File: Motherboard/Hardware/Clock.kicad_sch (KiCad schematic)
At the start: 18 parts, among them Q46 BC858, Q50 BC858, Q51 BC858

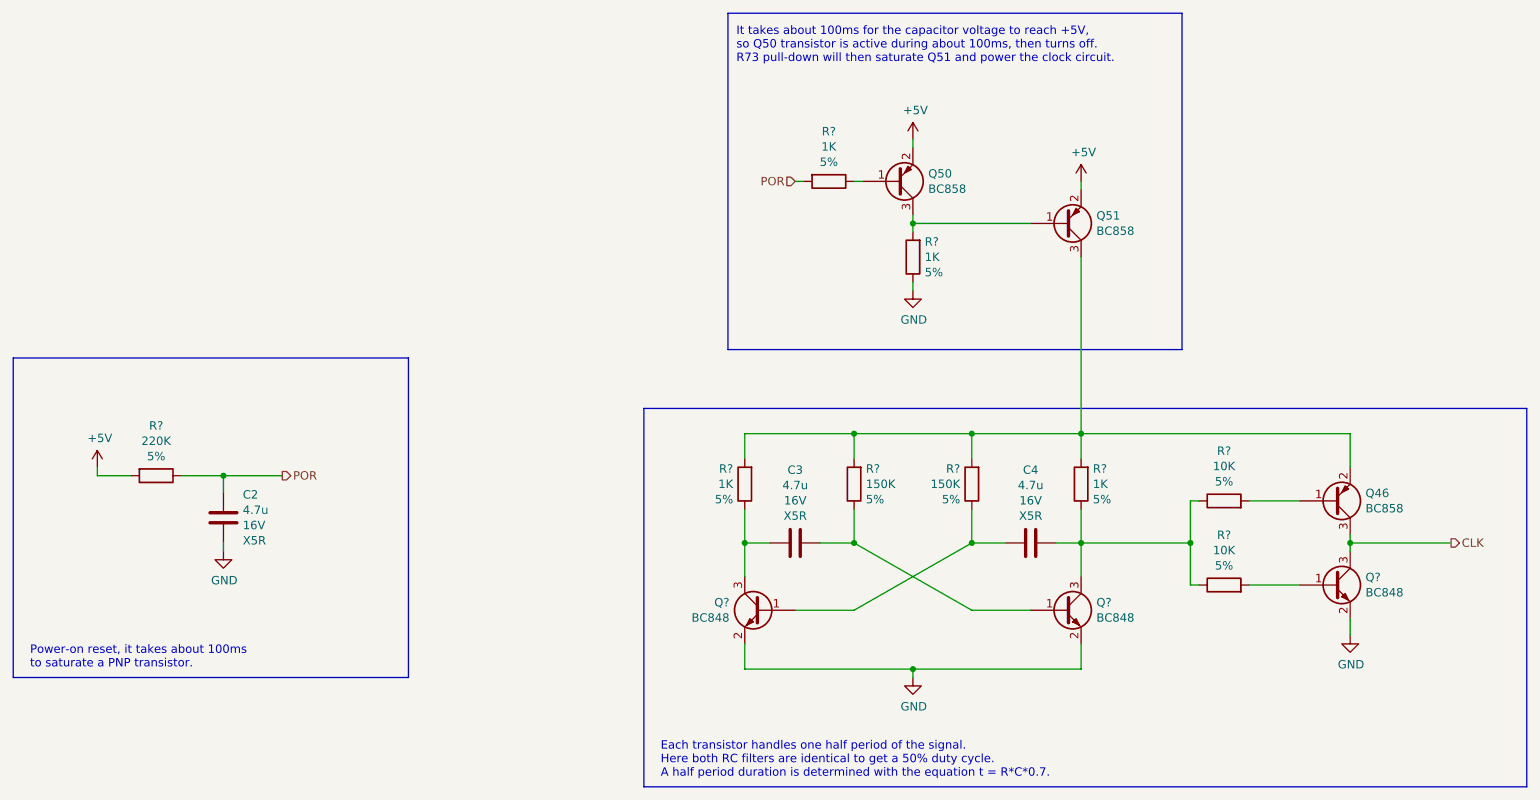
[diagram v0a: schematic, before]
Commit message: Updated the motherboard PCB to KiCad 7.
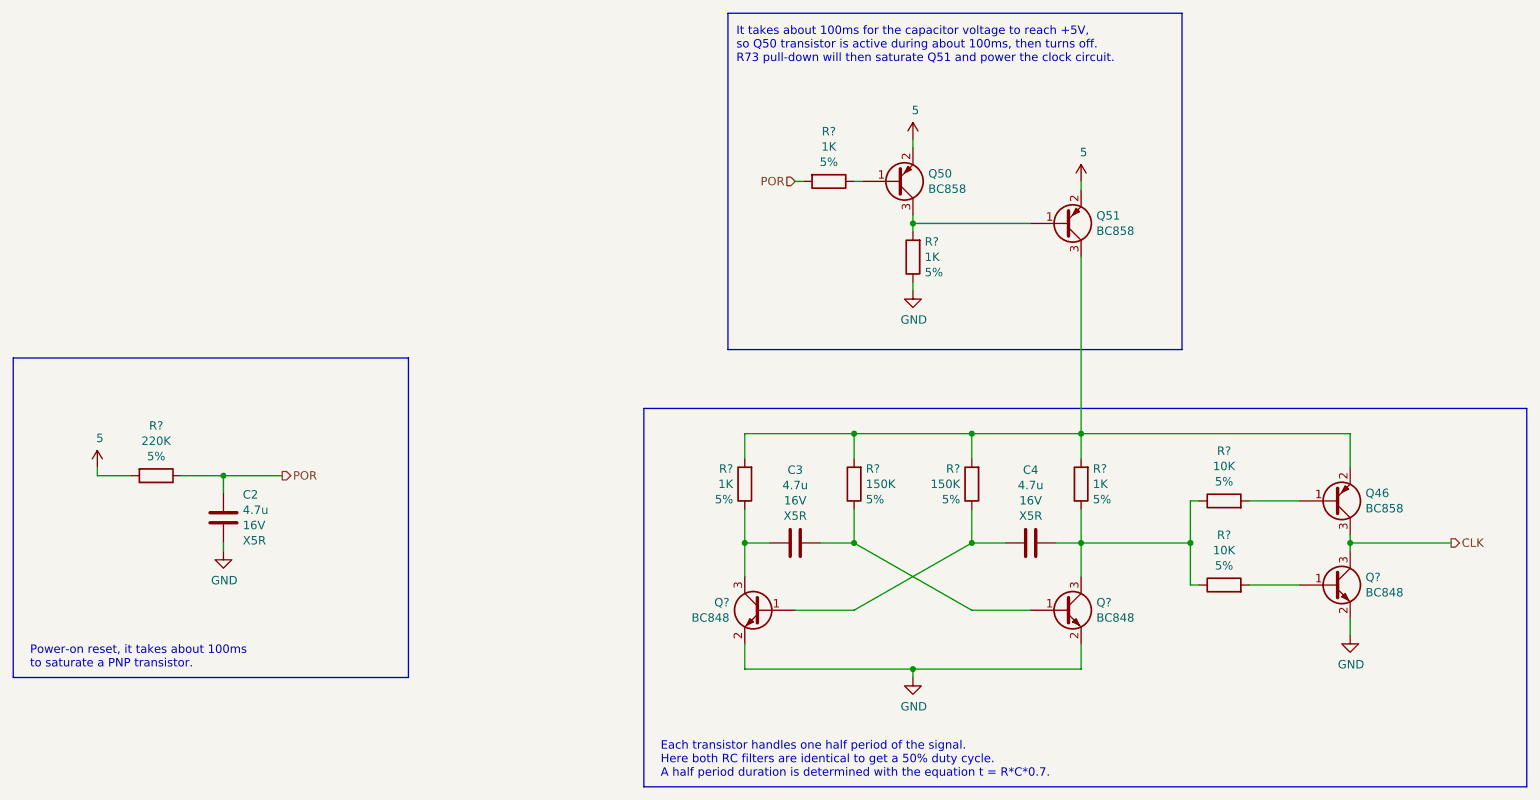
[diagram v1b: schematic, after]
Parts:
- Q46, Q50, Q51: Spice_Lib_File Spice_Simulation/BC858.lib -> (none); Spice_Model BC858 -> (none); Spice_Netlist_Enabled Y -> (none); Spice_Node_Sequence 3 1 2 -> (none); Spice_Primitive Q -> (none)
- Q? (x3): Spice_Lib_File Spice_Simulation/BC848.lib -> (none); Spice_Model BC848 -> (none); Spice_Netlist_Enabled Y -> (none); Spice_Node_Sequence 3 1 2 -> (none); Spice_Primitive Q -> (none)
- R? (x9): Spice_Model 1k -> (none); Spice_Netlist_Enabled Y -> (none); Spice_Primitive R -> (none)
